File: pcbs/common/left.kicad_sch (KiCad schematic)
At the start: 88 parts

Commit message: Update for rev4.1.0
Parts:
- removed F?: BSMD0603-050-12V, Fuse:Fuse_0603_1608Metric, symbol Device:Fuse
- removed J?: ST-0277D00-052-142, kbd_local:ST-0277D00-052-142, symbol Connector_Audio:AudioJack4
- added J2: TRS, kbd_local:PJ-398A-5A_PJ-399B-6A, symbol Connector_Audio:AudioJack3
- added R?: 10K, Resistor_SMD:R_0402_1005Metric, symbol Device:R_Small
- added R?: 5.6k, Resistor_SMD:R_0402_1005Metric, symbol Device:R_Small
- ZD?: value ESD5Z5V0C -> RB521S30T1G; JLCPCB Part # C2901325 -> C145179
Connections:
- net +5V: now also ZD?.1 (K), J2.T
- net GND: now also J2.S, R?.2; no longer ZD?.2 (A)
- net TX: now also J2.R
- net VBUS: now also ZD?.2 (A), R?.1; no longer ZD?.1 (K)
- net RX renamed USB_VBUS_PIN
- net USB_VBUS_PIN: now also R?.1, R?.2
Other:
- note added: "TRS"
- note removed: "T(4,5), R1(3), R2(2), S(1)"
- note removed: "TRRS"
- note removed: "left R1:RX, R2:TX right R1:TX, R2:RX"
- moved on the sheet: ZD?

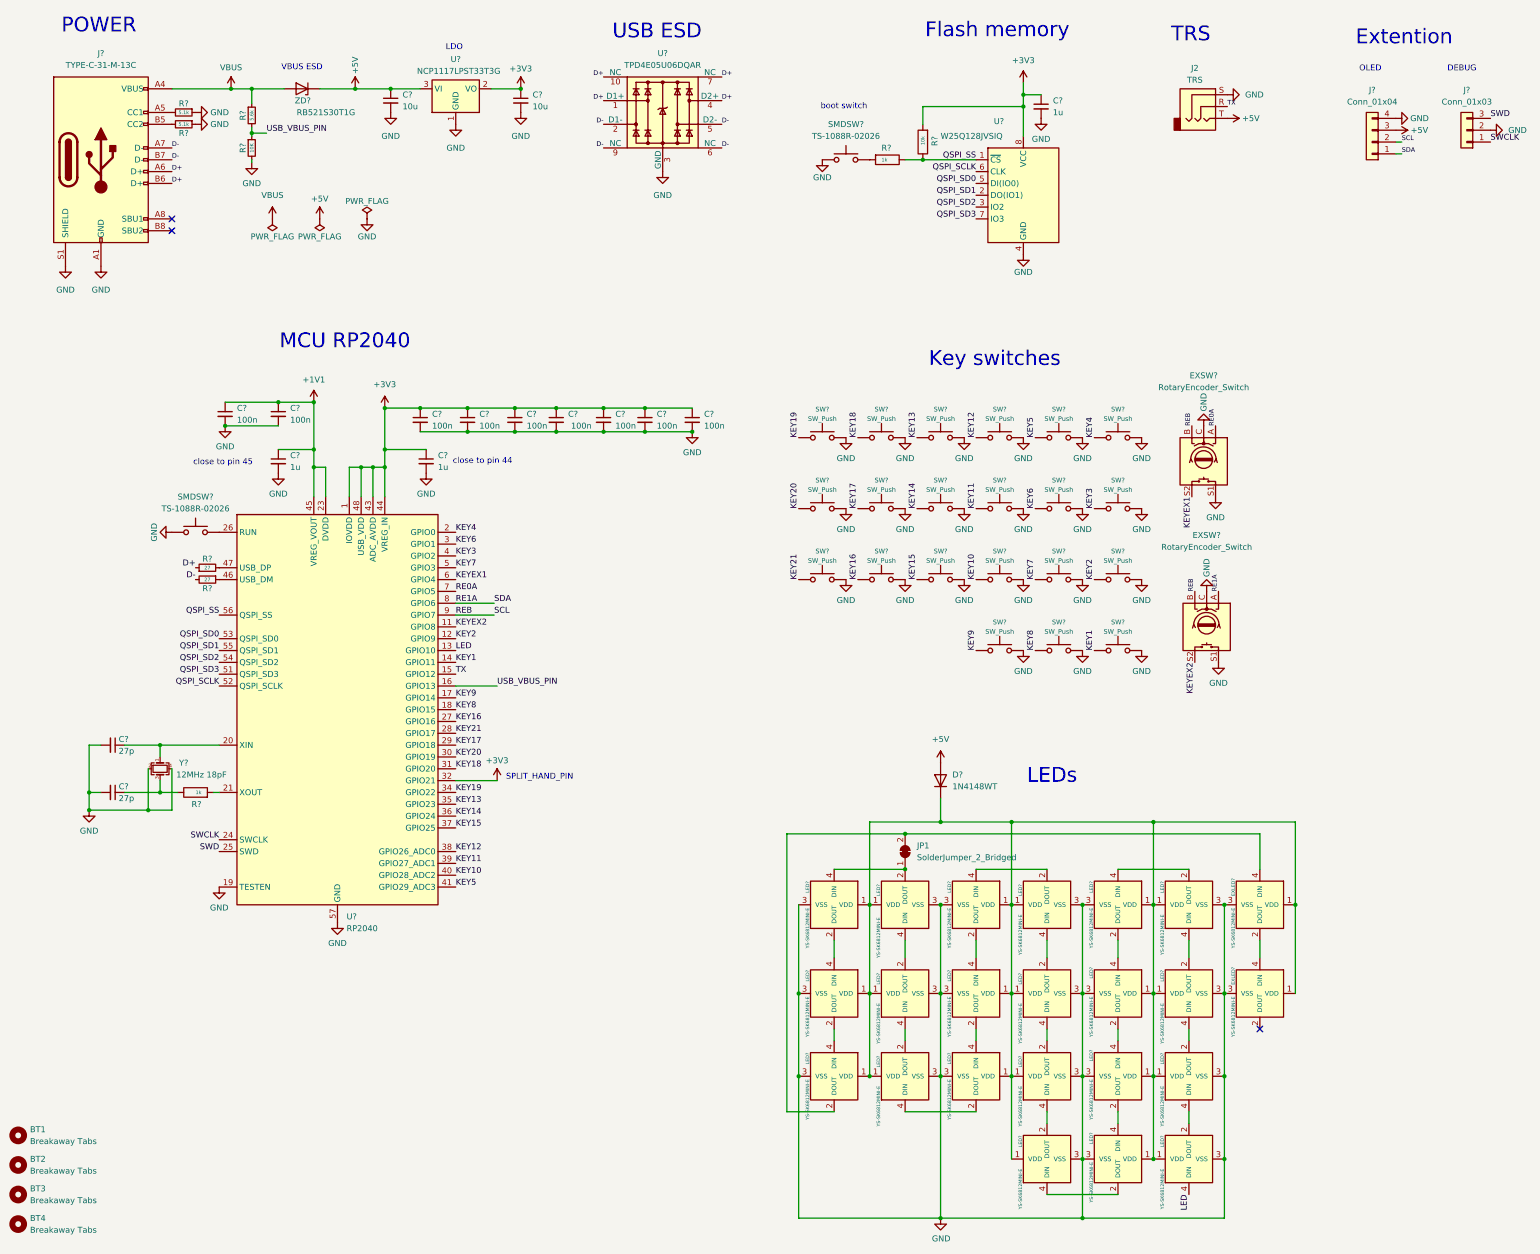
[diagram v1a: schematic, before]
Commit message: Move MCU to the center of the PCB
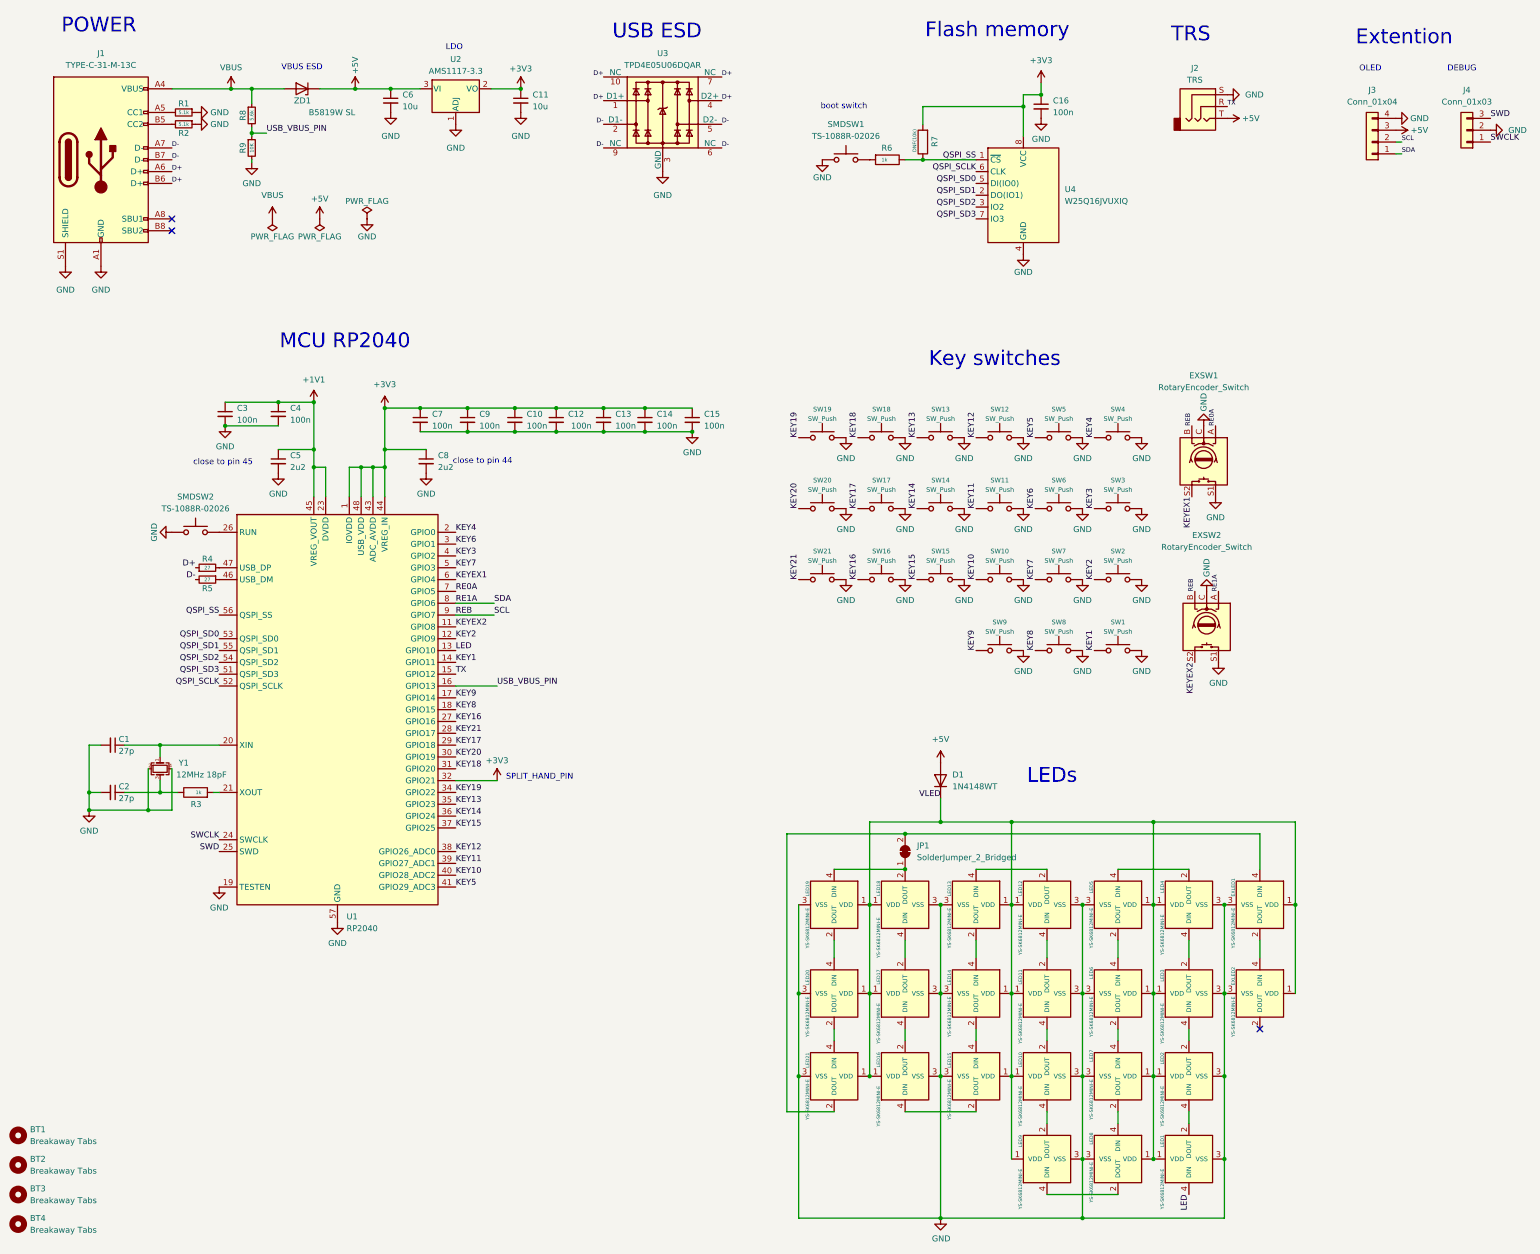
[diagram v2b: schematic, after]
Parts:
- removed U?: W25Q128JVSIQ, Package_SO:SOIC-8_5.23x5.23mm_P1.27mm, symbol Memory_Flash:W25Q128JVS
- removed U?: NCP1117LPST33T3G, Package_TO_SOT_SMD:SOT-223-3_TabPin2, symbol Regulator_Linear:NCP1117-3.3_SOT223
- added U2: AMS1117-3.3, Package_TO_SOT_SMD:SOT-89-3, symbol Regulator_Linear:LM317L_SOT-89
- added U4: W25Q16JVUXIQ, Package_SON:Winbond_USON-8-1EP_3x2mm_P0.5mm_EP0.2x1.6mm, symbol Memory_Flash:W25Q16JVSS
- C1, C10, C12, C13, C14, C15, C2, C3, C4, C7, C9: renamed from C?; footprint Capacitor_SMD:C_0402_1005Metric -> Capacitor_SMD:C_0201_0603Metric
- C11, C6: renamed from C?; footprint Capacitor_SMD:C_0402_1005Metric -> Capacitor_SMD:C_0805_2012Metric
- C16: renamed from C?; value 1u -> 100n; footprint Capacitor_SMD:C_0402_1005Metric -> Capacitor_SMD:C_0201_0603Metric
- C5, C8: renamed from C?; value 1u -> 2u2
- D1: renamed from D?; footprint Diode_SMD:D_SOD-523 -> Diode_SMD:D_SOD-323
- R1, R2: renamed from R?; footprint Resistor_SMD:R_0402_1005Metric -> Resistor_SMD:R_0201_0603Metric; LCSC (none) -> C25905
- R4, R5: renamed from R?; footprint Resistor_SMD:R_0402_1005Metric -> Capacitor_SMD:C_0201_0603Metric
- R7: renamed from R?; value 10k -> DNF(10k)
- ZD1: renamed from ZD?; value RB521S30T1G -> B5819W SL; footprint Diode_SMD:D_SOD-523 -> Diode_SMD:D_SOD-123; JLCPCB Part # C145179 -> C8598
- gave numbers to parts that had none: 58
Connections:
- net +3V3: now also U2.2 (VO), U4.8 (VCC)
- net +5V: now also U2.3 (VI)
- net GND: now also U2.1 (ADJ), U4.4 (GND)
- net QSPI_SCLK: now also U4.6 (CLK)
- net QSPI_SD0: now also U4.5 (DI(IO0))
- net QSPI_SD1: now also U4.2 (DO(IO1))
- net QSPI_SD2: now also U4.3 (IO2)
- net QSPI_SD3: now also U4.7 (IO3)
- net QSPI_SS: now also U4.1 (~{CS})
- net VLED: now reaches D1.1 (K), EXLED1.1 (VDD), EXLED2.1 (VDD), LED1.1 (VDD), LED10.1 (VDD), LED11.1 (VDD), LED12.1 (VDD), LED13.1 (VDD), LED14.1 (VDD), LED15.1 (VDD), LED16.1 (VDD), LED17.1 (VDD), LED18.1 (VDD), LED19.1 (VDD), LED2.1 (VDD), LED20.1 (VDD), LED21.1 (VDD), LED3.1 (VDD), LED4.1 (VDD), LED5.1 (VDD), LED6.1 (VDD), LED7.1 (VDD), LED8.1 (VDD), LED9.1 (VDD)

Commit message: Generate production files
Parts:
- BT1, BT2, BT3, BT4, J3, J4, JP1: now left out of the parts list
- C1, C2: LCSC Part # (none) -> C85899
- C10, C12, C13, C14, C15, C16, C3, C4, C7, C9: LCSC Part # (none) -> C76939
- C11, C6: LCSC Part # (none) -> C15850
- C5, C8: value 2u2 -> 1u; LCSC Part # (none) -> C52923
- D1: value 1N4148WT -> 1N4148W; JLCPCB Part # C232841 -> C2128
- EXLED1, EXLED2, LED1, LED10, LED11, LED12, LED13, LED14, LED15, LED16, LED17, LED18, LED19, LED2, LED20, LED21, LED3, LED4, LED5, LED6, LED7, LED8, LED9: LCSC Part # (none) -> C5149201
- R1, R2: LCSC C25905 -> (none); LCSC Part # (none) -> C270344
- R3, R6: LCSC Part # (none) -> C11702
- R4, R5: LCSC Part # (none) -> C270320
- R7, R9: LCSC Part # (none) -> C25744
- R8: LCSC Part # (none) -> C25908
- SW1: footprint kbd:keyswitch_cherrymx_hotswap_1.5u -> kbd_local:keyswitch_cherrymx_hotswap_1.5u
- SW10, SW11, SW12, SW13, SW14, SW15, SW16, SW17, SW18, SW19, SW2, SW20, SW21, SW3, SW4, SW5, SW6, SW7, SW8, SW9: footprint kbd:keyswitch_cherrymx_hotswap_1u -> kbd_local:keyswitch_cherrymx_hotswap_1u

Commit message: Add Corne Chocolate v4.1.1
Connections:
- net GND: now also EXSW1.S2, EXSW2.S2; no longer EXSW1.S1, EXSW2.S1
- net KEYEX1: now also EXSW1.S1; no longer EXSW1.S2
- net KEYEX2: now also EXSW2.S1; no longer EXSW2.S2
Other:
- moved on the sheet: EXSW1
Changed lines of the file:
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@@
 	)
 	(label "RE0A"
-		(at 274.955 105.41 90)
+		(at 274.32 105.41 90)
 		(fields_autoplaced yes)
 		(effects
@@
 		)
 	)
+	(label "KEYEX1"
+		(at 274.32 120.65 270)
+		(fields_autoplaced yes)
+		(effects
+			(font
+				(size 1.27 1.27)
+			)
+			(justify right bottom)
+		)
+	)
 	(label "LED"
 		(at 111.76 153.67 0)
@@
 		)
 	)
+	(label "KEYEX2"
+		(at 275.59 156.21 270)
+		(fields_autoplaced yes)
+		(effects
+			(font
+				(size 1.27 1.27)
+			)
+			(justify right bottom)
+		)
+	)
 	(label "SCL"
 		(at 120.015 146.05 0)
@@
 		)
 	)
-	(label "KEYEX1"
-		(at 269.875 120.65 270)
-		(fields_autoplaced yes)
-		(effects
-			(font
-				(size 1.27 1.27)
-			)
-			(justify right bottom)
-		)
-	)
 	(label "KEY7"
 		(at 236.22 138.43 90)
@@
 		)
 	)
-	(label "KEYEX2"
-		(at 270.51 156.21 270)
-		(fields_autoplaced yes)
-		(effects
-			(font
-				(size 1.27 1.27)
-			)
-			(justify right bottom)
-		)
-	)
 	(label "KEY15"
 		(at 210.82 138.43 90)
@@
 	)
 	(label "REB"
-		(at 269.875 105.41 90)
+		(at 269.24 105.41 90)
 		(fields_autoplaced yes)
 		(effects
@@
 	)
 	(symbol
-		(lib_id "power:GND")
-		(at 274.955 120.65 0)
-		(unit 1)
-		(exclude_from_sim no)
-		(in_bom yes)
-		(on_board yes)
-		(dnp no)
-		(fields_autoplaced yes)
-		(property "Reference" "#PWR056"
-			(at 274.955 127 0)
-			(effects
-				(font
-					(size 1.27 1.27)
-				)
-				(hide yes)
-			)
-		)
-		(property "Value" "GND"
-			(at 274.955 125.095 0)
-			(effects
-				(font
-					(size 1.27 1.27)
-				)
-			)
-		)
-		(property "Footprint" ""
-			(at 274.955 120.65 0)
-			(effects
-				(font
-					(size 1.27 1.27)
-				)
-				(hide yes)
-			)
-		)
-		(property "Datasheet" ""
-			(at 274.955 120.65 0)
-			(effects
-				(font
-					(size 1.27 1.27)
-				)
-				(hide yes)
-			)
-		)
-		(property "Description" ""
-			(at 274.955 120.65 0)
-			(effects
-				(font
-					(size 1.27 1.27)
-				)
-				(hide yes)
-			)
-		)
-		(pin "1"
-		)
-		(instances
-			(project "corne-cherry"
-				(path "/4cc5d416-57f5-4147-8183-e03ae6b1198a/089db7cd-2934-428b-a62a-55e0735649ba"
-					(reference "#PWR056")
-					(unit 1)
-				)
-			)
-		)
-	)
-	(symbol
 		(lib_id "Device:R_Small")
 		(at 58.42 138.43 270)
@@
 	)
 	(symbol
-		(lib_id "power:GND")
-		(at 275.59 156.21 0)
-		(unit 1)
-		(exclude_from_sim no)
-		(in_bom yes)
-		(on_board yes)
-		(dnp no)
-		(fields_autoplaced yes)
-		(property "Reference" "#PWR059"
-			(at 275.59 162.56 0)
-			(effects
-				(font
-					(size 1.27 1.27)
-				)
-				(hide yes)
-			)
-		)
-		(property "Value" "GND"
-			(at 275.59 160.655 0)
-			(effects
-				(font
-					(size 1.27 1.27)
-				)
-			)
-		)
-		(property "Footprint" ""
-			(at 275.59 156.21 0)
-			(effects
-				(font
-					(size 1.27 1.27)
-				)
-				(hide yes)
-			)
-		)
-		(property "Datasheet" ""
-			(at 275.59 156.21 0)
-			(effects
-				(font
-					(size 1.27 1.27)
-				)
-				(hide yes)
-			)
-		)
-		(property "Description" ""
-			(at 275.59 156.21 0)
-			(effects
-				(font
-					(size 1.27 1.27)
-				)
-				(hide yes)
-			)
-		)
-		(pin "1"
-		)
-		(instances
-			(project "corne-cherry"
-				(path "/4cc5d416-57f5-4147-8183-e03ae6b1198a/089db7cd-2934-428b-a62a-55e0735649ba"
-					(reference "#PWR059")
-					(unit 1)
-				)
-			)
-		)
-	)
-	(symbol
 		(lib_id "kbd_local:YS-SK6812MINI-E")
 		(at 284.48 208.28 270)
@@
 	(symbol
 		(lib_id "power:GND")
-		(at 272.415 105.41 180)
+		(at 271.78 105.41 180)
 		(unit 1)
 		(exclude_from_sim no)
@@
 		(dnp no)
 		(property "Reference" "#PWR054"
-			(at 272.415 99.06 0)
+			(at 271.78 99.06 0)
 			(effects
 				(font
@@
 		)
 		(property "Value" "GND"
-			(at 272.415 100.33 90)
+			(at 271.78 100.33 90)
 			(effects
 				(font
@@
 		)
 		(property "Footprint" ""
-			(at 272.415 105.41 0)
+			(at 271.78 105.41 0)
 			(effects
 				(font
@@
 		)
 		(property "Datasheet" ""
-			(at 272.415 105.41 0)
+			(at 271.78 105.41 0)
 			(effects
 				(font
@@
 		)
 		(property "Description" ""
-			(at 272.415 105.41 0)
+			(at 271.78 105.41 0)
 			(effects
 				(font
@@
 	(symbol
 		(lib_id "power:GND")
+		(at 270.51 156.21 0)
+		(unit 1)
+		(exclude_from_sim no)
+		(in_bom yes)
+		(on_board yes)
+		(dnp no)
+		(fields_autoplaced yes)
+		(property "Reference" "#PWR057"
+			(at 270.51 162.56 0)
+			(effects
+				(font
+					(size 1.27 1.27)
+				)
+				(hide yes)
+			)
+		)
+		(property "Value" "GND"
+			(at 270.51 160.655 0)
+			(effects
+				(font
+					(size 1.27 1.27)
+				)
+			)
+		)
+		(property "Footprint" ""
+			(at 270.51 156.21 0)
+			(effects
+				(font
+					(size 1.27 1.27)
+				)
+				(hide yes)
+			)
+		)
+		(property "Datasheet" ""
+			(at 270.51 156.21 0)
+			(effects
+				(font
+					(size 1.27 1.27)
+				)
+				(hide yes)
+			)
+		)
+		(property "Description" ""
+			(at 270.51 156.21 0)
+			(effects
+				(font
+					(size 1.27 1.27)
+				)
+				(hide yes)
+			)
+		)
+		(pin "1"
+		)
+		(instances
+			(project "corne-chocolate"
+				(path "/4cc5d416-57f5-4147-8183-e03ae6b1198a/089db7cd-2934-428b-a62a-55e0735649ba"
+					(reference "#PWR057")
+					(unit 1)
+				)
+			)
+		)
+	)
+	(symbol
+		(lib_id "power:GND")
 		(at 195.58 123.19 0)
 		(unit 1)
@@
 	)
 	(symbol
+		(lib_id "power:GND")
+		(at 269.24 120.65 0)
+		(unit 1)
+		(exclude_from_sim no)
+		(in_bom yes)
+		(on_board yes)
+		(dnp no)
+		(fields_autoplaced yes)
+		(property "Reference" "#PWR056"
+			(at 269.24 127 0)
+			(effects
+				(font
+					(size 1.27 1.27)
+				)
+				(hide yes)
+			)
+		)
+		(property "Value" "GND"
+			(at 269.24 125.095 0)
+			(effects
+				(font
+					(size 1.27 1.27)
+				)
+			)
+		)
+		(property "Footprint" ""
+			(at 269.24 120.65 0)
+			(effects
+				(font
+					(size 1.27 1.27)
+				)
+				(hide yes)
+			)
+		)
+		(property "Datasheet" ""
+			(at 269.24 120.65 0)
+			(effects
+				(font
+					(size 1.27 1.27)
+				)
+				(hide yes)
+			)
+		)
+		(property "Description" ""
+			(at 269.24 120.65 0)
+			(effects
+				(font
+					(size 1.27 1.27)
+				)
+				(hide yes)
+			)
+		)
+		(pin "1"
+		)
+		(instances
+			(project "corne-chocolate"
+				(path "/4cc5d416-57f5-4147-8183-e03ae6b1198a/089db7cd-2934-428b-a62a-55e0735649ba"
+					(reference "#PWR056")
+					(unit 1)
+				)
+			)
+		)
+	)
+	(symbol
 		(lib_id "Device:C_Small")
 		(at 105.41 113.03 0)
@@
 	(symbol
 		(lib_id "Device:RotaryEncoder_Switch")
-		(at 272.415 113.03 270)
+		(at 271.78 113.03 270)
 		(unit 1)
 		(exclude_from_sim no)
@@
 		(dnp no)
 		(property "Reference" "EXSW1"
-			(at 272.415 94.615 90)
+			(at 271.78 94.615 90)
 			(effects
 				(font
@@
 		)
 		(property "Value" "RotaryEncoder_Switch"
-			(at 272.415 97.155 90)
+			(at 271.78 97.155 90)
 			(effects
 				(font
@@
 		)
 		(property "Footprint" "kbd_local:keyswitch_cherrymx_hotswap_1u_rotary_encoder_ec12"
-			(at 276.479 109.22 0)
+			(at 275.844 109.22 0)
 			(effects
 				(font
@@
 		)
 		(property "Datasheet" "~"
-			(at 279.019 113.03 0)
+			(at 278.384 113.03 0)
 			(effects
 				(font
@@
 		)
 		(property "Description" ""
-			(at 272.415 113.03 0)
+			(at 271.78 113.03 0)
 			(effects
 				(font
